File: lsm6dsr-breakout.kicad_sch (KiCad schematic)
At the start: 15 parts, among them CN1 AFC10-S04QCA-00, CN2 AFC10-S04QCA-00, J1 Conn_01x06_Pin, J2 Conn_01x04_Pin, U1 LSM6DSRTR

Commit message: beautify schematic
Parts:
- added R6: 2.2k, Resistor_SMD:R_0402_1005Metric, symbol Device:R
- R1, R2, R3, R4, R5: value 3.9k -> 2.2k
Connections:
- net CS: now also R5.2
- net GND: now also C1.2; no longer C1.1
- net SCL: now also R1.2; no longer R4.1
- net SDA: now also R2.2; no longer R3.1
- net SDO: now also R6.2; no longer R5.2
- net VDD: now also C1.1, R3.1, R4.1, R6.1; no longer C1.2, R3.2, R4.2
- net XCL: now also R3.2; no longer R1.2
- net XDA: now also R4.2; no longer R2.2
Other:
- moved on the sheet: CN1, CN2, H1, H2, J1, J2, JP1, U1

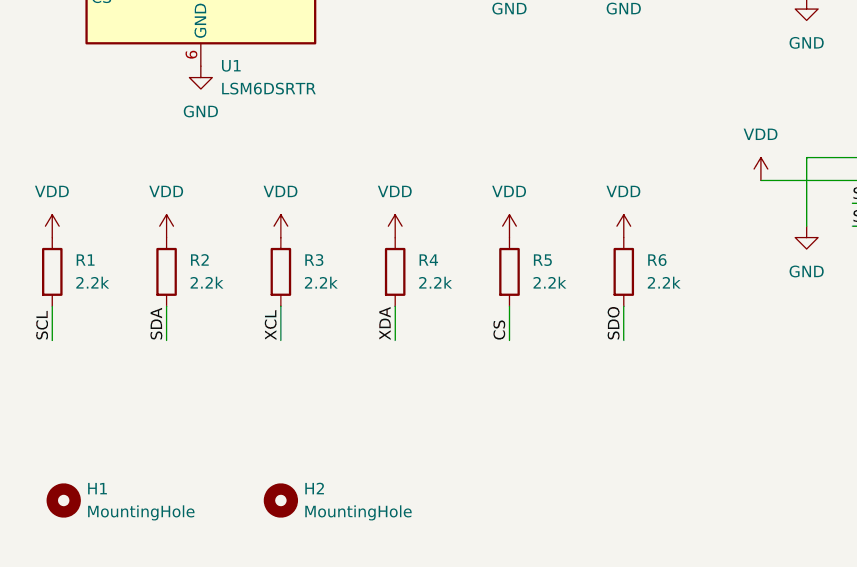
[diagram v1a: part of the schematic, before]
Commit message: use higher pullups, make it dippable, comply MEMS design guideline
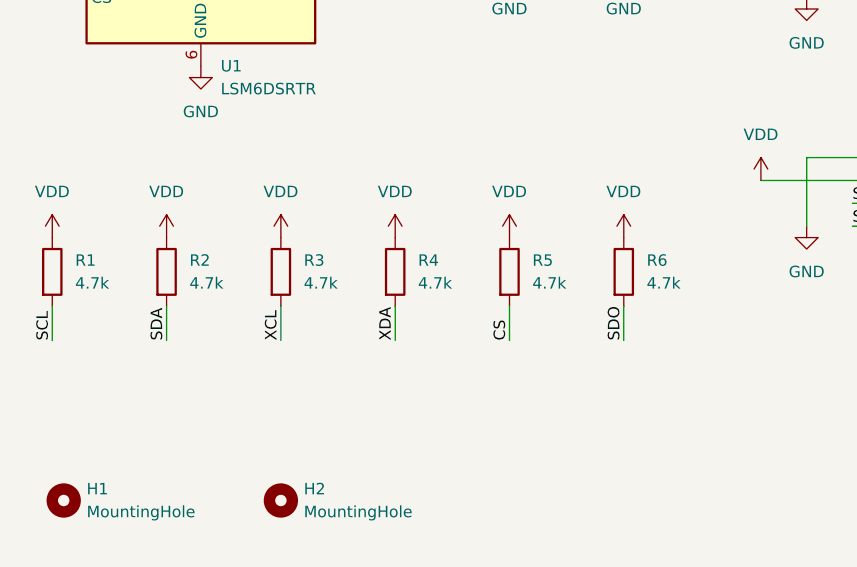
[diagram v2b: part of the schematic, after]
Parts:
- R1, R2, R3, R4, R5, R6: value 2.2k -> 4.7k
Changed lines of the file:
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@@
 			)
 		)
-		(property "Value" "2.2k"
+		(property "Value" "4.7k"
 			(at 53.34 77.4699 0)
 			(effects
@@
 			)
 		)
-		(property "Value" "2.2k"
+		(property "Value" "4.7k"
 			(at 78.74 77.4699 0)
 			(effects
@@
 			)
 		)
-		(property "Value" "2.2k"
+		(property "Value" "4.7k"
 			(at 40.64 77.4699 0)
 			(effects
@@
 			)
 		)
-		(property "Value" "2.2k"
+		(property "Value" "4.7k"
 			(at 66.04 77.4699 0)
 			(effects
@@
 			)
 		)
-		(property "Value" "2.2k"
+		(property "Value" "4.7k"
 			(at 27.94 77.4699 0)
 			(effects
@@
 			)
 		)
-		(property "Value" "2.2k"
+		(property "Value" "4.7k"
 			(at 91.44 77.4699 0)
 			(effects
